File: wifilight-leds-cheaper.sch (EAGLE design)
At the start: 57 parts

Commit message: Damnit, how was I supposed to power this thing?
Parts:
- added +, -: (no value), adafruit:PINHD-1X1
- added D2: (no value), SparkFun-DiscreteSemi:DIODESOD123
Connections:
- new net N$18: +.1, D2.A
- net 12V: now also D2.C
- net GND: now also -.1
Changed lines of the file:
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@@
 <part name="R7" library="SparkFun-Passives" deviceset="RESISTOR" device="0402-RES" value="???"/>
 <part name="GND16" library="supply1" deviceset="GND" device=""/>
+<part name="+" library="adafruit" deviceset="PINHD-1X1" device=""/>
+<part name="-" library="adafruit" deviceset="PINHD-1X1" device=""/>
+<part name="D2" library="SparkFun-DiscreteSemi" deviceset="DIODE" device="SOD123"/>
+<part name="GND17" library="SparkFun-Aesthetics" deviceset="GND" device=""/>
+<part name="SUPPLY19" library="SparkFun-Aesthetics" deviceset="12V" device=""/>
 </parts>
 <sheets>
@@
 <instance part="R7" gate="G$1" x="17.78" y="114.3" rot="R270"/>
 <instance part="GND16" gate="1" x="17.78" y="93.98"/>
+<instance part="+" gate="G$1" x="-58.42" y="162.56"/>
+<instance part="-" gate="G$1" x="-58.42" y="147.32"/>
+<instance part="D2" gate="G$1" x="-76.2" y="162.56" rot="R180"/>
+<instance part="GND17" gate="1" x="-81.28" y="142.24"/>
+<instance part="SUPPLY19" gate="G$1" x="-86.36" y="165.1"/>
 </instances>
 <busses>
@@
 <wire x1="17.78" y1="96.52" x2="17.78" y2="99.06" width="0.1524" layer="91"/>
 </segment>
+<segment>
+<pinref part="-" gate="G$1" pin="1"/>
+<wire x1="-60.96" y1="147.32" x2="-81.28" y2="147.32" width="0.1524" layer="91"/>
+<pinref part="GND17" gate="1" pin="GND"/>
+<wire x1="-81.28" y1="147.32" x2="-81.28" y2="144.78" width="0.1524" layer="91"/>
+</segment>
 </net>
 <net name="SCL" class="0">
@@
 <pinref part="SUPPLY8" gate="G$1" pin="12V"/>
 <wire x1="-10.16" y1="116.84" x2="-10.16" y2="121.92" width="0.1524" layer="91"/>
+</segment>
+<segment>
+<pinref part="SUPPLY19" gate="G$1" pin="12V"/>
+<wire x1="-86.36" y1="165.1" x2="-86.36" y2="162.56" width="0.1524" layer="91"/>
+<pinref part="D2" gate="G$1" pin="C"/>
+<wire x1="-86.36" y1="162.56" x2="-78.74" y2="162.56" width="0.1524" layer="91"/>
 </segment>
 </net>
@@
 </segment>
 </net>
+<net name="N$18" class="0">
+<segment>
+<pinref part="D2" gate="G$1" pin="A"/>
+<pinref part="+" gate="G$1" pin="1"/>
+<wire x1="-73.66" y1="162.56" x2="-60.96" y2="162.56" width="0.1524" layer="91"/>
+</segment>
+</net>

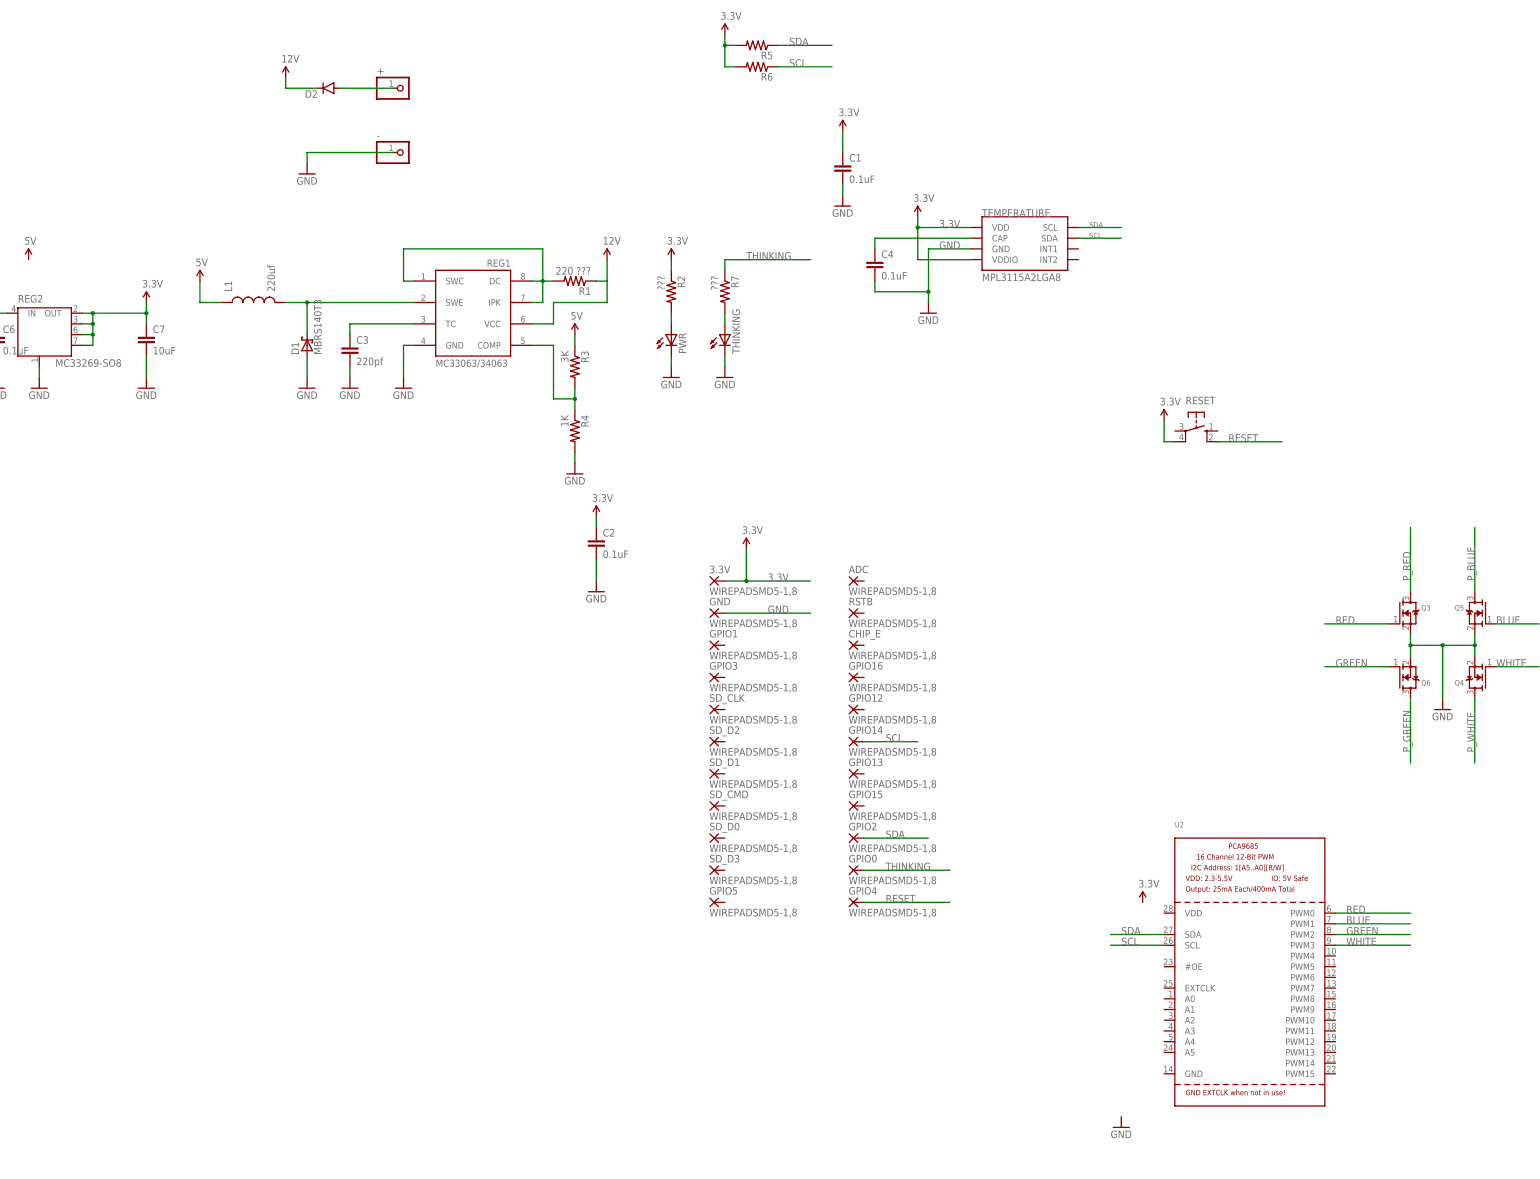
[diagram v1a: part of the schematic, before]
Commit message: As ordered recently. Discovered that SOT-23's are puny and 4 Luxeon Rebels are overkill. And that Banggood has cheaper ESP8266 modules.
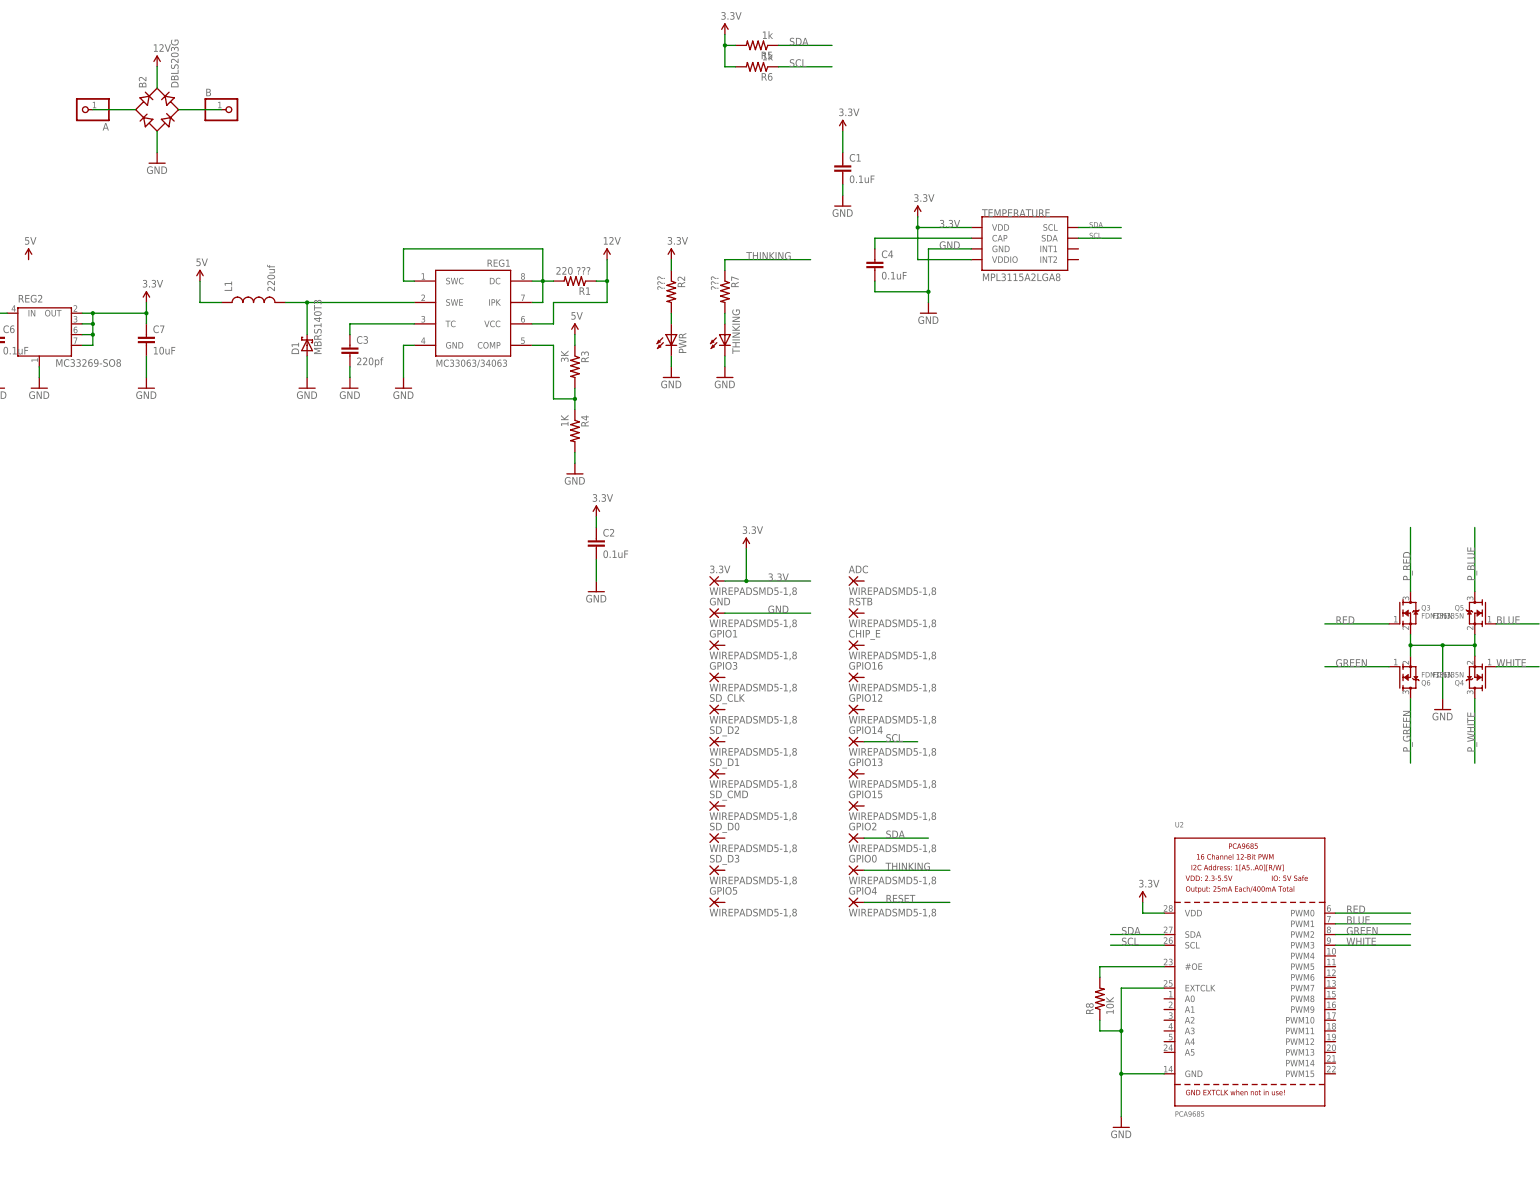
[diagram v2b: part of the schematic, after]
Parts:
- removed +, -: (no value), adafruit:PINHD-1X1
- removed D2: (no value), SparkFun-DiscreteSemi:DIODESOD123
- removed RESET: (no value), switch-omron:10-XX
- added A, B: (no value), adafruit:PINHD-1X1
- added B2: DBLS203G, rectifier:DBLS203G
- added R8: 10K, SparkFun-Resistors:10KOHM-1/10W-1%(0603)0603
- Q3, Q4, Q5, Q6: value (none) -> FDN335N
- R5, R6: value (none) -> 1k
- U2: value (none) -> PCA9685
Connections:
- new net N$19: B.1, B2.AC2
- new net N$20: R8.2, U2.#OE
- net 12V: now also B2.+; no longer D2.C
- net 3.3V: now also U2.VDD; no longer RESET.P1
- net GND: now also B2.-, R8.1, U2.EXTCLK, U2.GND; no longer -.1
- net N$18: now also A.1, B2.AC1; no longer +.1, D2.A
- net RESET: no longer RESET.S1
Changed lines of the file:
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@@
 <parts>
 <part name="C1" library="SparkFun-Passives" deviceset="CAP" device="0402-CAP" value="0.1uF"/>
-<part name="R5" library="SparkFun-Passives" deviceset="RESISTOR" device="0402-RES"/>
-<part name="R6" library="SparkFun-Passives" deviceset="RESISTOR" device="0402-RES"/>
+<part name="R5" library="SparkFun-Passives" deviceset="RESISTOR" device="0402-RES" value="1k"/>
+<part name="R6" library="SparkFun-Passives" deviceset="RESISTOR" device="0402-RES" value="1k"/>
 <part name="GND5" library="supply1" deviceset="GND" device=""/>
 <part name="3.3V" library="wirepad" deviceset="WIREPAD" device="SMD5-1,8"/>
@@
 <part name="GPIO0" library="wirepad" deviceset="WIREPAD" device="SMD5-1,8"/>
 <part name="GPIO4" library="wirepad" deviceset="WIREPAD" device="SMD5-1,8"/>
-<part name="U2" library="adafruit" deviceset="PCA9685" device=""/>
+<part name="U2" library="adafruit" deviceset="PCA9685" device="" value="PCA9685"/>
 <part name="GND1" library="SparkFun-Aesthetics" deviceset="GND" device=""/>
-<part name="Q3" library="adafruit" deviceset="MOSFET-N" device="WAVE"/>
-<part name="Q4" library="adafruit" deviceset="MOSFET-N" device="WAVE"/>
-<part name="Q5" library="adafruit" deviceset="MOSFET-N" device="WAVE"/>
-<part name="Q6" library="adafruit" deviceset="MOSFET-N" device="WAVE"/>
+<part name="Q3" library="adafruit" deviceset="MOSFET-N" device="WAVE" value="FDN335N"/>
+<part name="Q4" library="adafruit" deviceset="MOSFET-N" device="WAVE" value="FDN335N"/>
+<part name="Q5" library="adafruit" deviceset="MOSFET-N" device="WAVE" value="FDN335N"/>
+<part name="Q6" library="adafruit" deviceset="MOSFET-N" device="WAVE" value="FDN335N"/>
 <part name="LED1" library="led" deviceset="OVSTRGBBCR8" device=""/>
 <part name="LED2" library="led" deviceset="OVSTRGBBCR8" device=""/>
@@
 <part name="SUPPLY16" library="SparkFun-Aesthetics" deviceset="3.3V" device=""/>
 <part name="SUPPLY17" library="SparkFun-Aesthetics" deviceset="3.3V" device=""/>
-<part name="RESET" library="switch-omron" deviceset="10-XX" device=""/>
-<part name="SUPPLY18" library="SparkFun-Aesthetics" deviceset="3.3V" device=""/>
 <part name="THINKING" library="led" deviceset="LED" device="CHIP-LED0805"/>
 <part name="R7" library="SparkFun-Passives" deviceset="RESISTOR" device="0402-RES" value="???"/>
 <part name="GND16" library="supply1" deviceset="GND" device=""/>
-<part name="+" library="adafruit" deviceset="PINHD-1X1" device=""/>
-<part name="-" library="adafruit" deviceset="PINHD-1X1" device=""/>
-<part name="D2" library="SparkFun-DiscreteSemi" deviceset="DIODE" device="SOD123"/>
+<part name="A" library="adafruit" deviceset="PINHD-1X1" device=""/>
+<part name="B" library="adafruit" deviceset="PINHD-1X1" device=""/>
 <part name="GND17" library="SparkFun-Aesthetics" deviceset="GND" device=""/>
 <part name="SUPPLY19" library="SparkFun-Aesthetics" deviceset="12V" device=""/>
+<part name="B2" library="rectifier" deviceset="DB?*G" device="LS20" technology="3"/>
+<part name="R8" library="SparkFun-Resistors" deviceset="10KOHM-1/10W-1%(0603)" device="0603" value="10K"/>
 </parts>
 <sheets>
@@
 <instance part="SUPPLY16" gate="G$1" x="45.72" y="152.4"/>
 <instance part="SUPPLY17" gate="G$1" x="17.78" y="175.26"/>
-<instance part="RESET" gate="1" x="129.54" y="81.28" rot="R270"/>
-<instance part="SUPPLY18" gate="G$1" x="121.92" y="83.82"/>
 <instance part="THINKING" gate="G$1" x="17.78" y="104.14"/>
 <instance part="R7" gate="G$1" x="17.78" y="114.3" rot="R270"/>
 <instance part="GND16" gate="1" x="17.78" y="93.98"/>
-<instance part="+" gate="G$1" x="-58.42" y="162.56"/>
-<instance part="-" gate="G$1" x="-58.42" y="147.32"/>
-<instance part="D2" gate="G$1" x="-76.2" y="162.56" rot="R180"/>
-<instance part="GND17" gate="1" x="-81.28" y="142.24"/>
-<instance part="SUPPLY19" gate="G$1" x="-86.36" y="165.1"/>
+<instance part="A" gate="G$1" x="-134.62" y="157.48" rot="R180"/>
+<instance part="B" gate="G$1" x="-99.06" y="157.48"/>
+<instance part="GND17" gate="1" x="-116.84" y="144.78"/>
+<instance part="SUPPLY19" gate="G$1" x="-116.84" y="167.64"/>
+<instance part="B2" gate="G$1" x="-116.84" y="157.48" rot="R90"/>
+<instance part="R8" gate="G$1" x="106.68" y="-53.34" rot="R90"/>
 </instances>
 <busses>
@@
 </segment>
 <segment>
-<pinref part="-" gate="G$1" pin="1"/>
-<wire x1="-60.96" y1="147.32" x2="-81.28" y2="147.32" width="0.1524" layer="91"/>
 <pinref part="GND17" gate="1" pin="GND"/>
-<wire x1="-81.28" y1="147.32" x2="-81.28" y2="144.78" width="0.1524" layer="91"/>
+<wire x1="-116.84" y1="152.4" x2="-116.84" y2="147.32" width="0.1524" layer="91"/>
+<pinref part="B2" gate="G$1" pin="-"/>
+</segment>
+<segment>
+<pinref part="U2" gate="G$1" pin="GND"/>
+<pinref part="GND3" gate="1" pin="GND"/>
+<wire x1="121.92" y1="-71.12" x2="111.76" y2="-71.12" width="0.1524" layer="91"/>
+<wire x1="111.76" y1="-71.12" x2="111.76" y2="-81.28" width="0.1524" layer="91"/>
+<pinref part="U2" gate="G$1" pin="EXTCLK"/>
+<wire x1="121.92" y1="-50.8" x2="111.76" y2="-50.8" width="0.1524" layer="91"/>
+<wire x1="111.76" y1="-50.8" x2="111.76" y2="-60.96" width="0.1524" layer="91"/>
+<pinref part="R8" gate="G$1" pin="1"/>
+<wire x1="111.76" y1="-60.96" x2="111.76" y2="-71.12" width="0.1524" layer="91"/>
+<wire x1="106.68" y1="-58.42" x2="106.68" y2="-60.96" width="0.1524" layer="91"/>
+<wire x1="106.68" y1="-60.96" x2="111.76" y2="-60.96" width="0.1524" layer="91"/>
+<junction x="111.76" y="-71.12"/>
+<junction x="111.76" y="-60.96"/>
 </segment>
 </net>
@@
 <pinref part="SUPPLY8" gate="G$1" pin="12V"/>
 <wire x1="-10.16" y1="116.84" x2="-10.16" y2="121.92" width="0.1524" layer="91"/>
-</segment>
-<segment>
+<junction x="-10.16" y="116.84"/>
+</segment>
+<segment>
+<wire x1="-116.84" y1="162.56" x2="-116.84" y2="167.64" width="0.1524" layer="91"/>
 <pinref part="SUPPLY19" gate="G$1" pin="12V"/>
-<wire x1="-86.36" y1="165.1" x2="-86.36" y2="162.56" width="0.1524" layer="91"/>
-<pinref part="D2" gate="G$1" pin="C"/>
-<wire x1="-86.36" y1="162.56" x2="-78.74" y2="162.56" width="0.1524" layer="91"/>
+<pinref part="B2" gate="G$1" pin="+"/>
 </segment>
 </net>
@@
 </segment>
 <segment>
-<pinref part="RESET" gate="1" pin="P1"/>
-<wire x1="124.46" y1="78.74" x2="121.92" y2="78.74" width="0.1524" layer="91"/>
-<pinref part="SUPPLY18" gate="G$1" pin="3.3V"/>
-<wire x1="121.92" y1="78.74" x2="121.92" y2="83.82" width="0.1524" layer="91"/>
+<pinref part="U2" gate="G$1" pin="VDD"/>
+<wire x1="121.92" y1="-33.02" x2="116.84" y2="-33.02" width="0.1524" layer="91"/>
+<pinref part="SUPPLY5" gate="G$1" pin="3.3V"/>
+<wire x1="116.84" y1="-33.02" x2="116.84" y2="-30.48" width="0.1524" layer="91"/>
 </segment>
 </net>
@@
 <net name="RESET" class="0">
 <segment>
-<pinref part="RESET" gate="1" pin="S1"/>
-<wire x1="134.62" y1="78.74" x2="149.86" y2="78.74" width="0.1524" layer="91"/>
-<label x="137.16" y="78.74" size="1.778" layer="95"/>
-</segment>
-<segment>
 <pinref part="GPIO4" gate="G$1" pin="P"/>
 <wire x1="50.8" y1="-30.48" x2="71.12" y2="-30.48" width="0.1524" layer="91"/>
@@
 </segment>
 </net>
+<net name="N$19" class="0">
+<segment>
+<pinref part="B" gate="G$1" pin="1"/>
+<wire x1="-111.76" y1="157.48" x2="-101.6" y2="157.48" width="0.1524" layer="91"/>
+<pinref part="B2" gate="G$1" pin="AC2"/>
+</segment>
+</net>
 <net name="N$18" class="0">
 <segment>
-<pinref part="D2" gate="G$1" pin="A"/>
-<pinref part="+" gate="G$1" pin="1"/>
-<wire x1="-73.66" y1="162.56" x2="-60.96" y2="162.56" width="0.1524" layer="91"/>
-</segment>
-</net>
+<pinref part="A" gate="G$1" pin="1"/>
+<wire x1="-132.08" y1="157.48" x2="-121.92" y2="157.48" width="0.1524" layer="91"/>
+<pinref part="B2" gate="G$1" pin="AC1"/>
+</segment>
+</net>
+<net name="N$20" class="0">
+<segment>
+<pinref part="U2" gate="G$1" pin="#OE"/>
+<wire x1="121.92" y1="-45.72" x2="106.68" y2="-45.72" width="0.1524" layer="91"/>
+<pinref part="R8" gate="G$1" pin="2"/>
+<wire x1="106.68" y1="-45.72" x2="106.68" y2="-48.26" width="0.1524" layer="91"/>
+</segment>
+</net>

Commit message: Mk2
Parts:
- removed 3.3V, ADC, CHIP_E, GND, GPIO0, GPIO1, GPIO12, GPIO13, GPIO14, GPIO15, GPIO16, GPIO2, GPIO3, GPIO4, GPIO5, RSTB, SD_CLK, SD_CMD, SD_D0, SD_D1, SD_D2, SD_D3: WIREPADSMD5-1,8, wirepad:WIREPADSMD5-1,8
- removed LED4: OVSTRGBBCR8, led:OVSTRGBBCR8
- removed Q5, Q6: FDN335N, adafruit:MOSFET-NWAVE
- removed U$4: LUXEON-REBEL, SparkFun-LED:LUXEON-REBEL
- added MPU: ESP8266_ESP-12, ESP8266-ESP12:ESP8266_ESP-12
- added Q1, Q2: BUK98180-100A, nxp_60:BUK98180-100A
- C1, C2, C3: device SparkFun-Passives:CAP0402-CAP -> resistor:C-EUC0805K
- C4, C6: device SparkFun-Capacitors:0.1UF-16V(+-10%)(0402) -> resistor:C-EUC0805K
- C7: device SparkFun-Capacitors:10UF-6.3V-20%(1206) -> resistor:C-EUC0805K
- Q3, Q4: value FDN335N -> BUK98180-100A; device adafruit:MOSFET-NWAVE -> nxp_60:BUK98180-100A
- R1, R2, R3, R4, R5, R6, R7: device SparkFun-Passives:RESISTOR0402-RES -> resistor:R-EU_R0805
- R8: device SparkFun-Resistors:10KOHM-1/10W-1%(0603)0603 -> resistor:R-EU_R0805
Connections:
- removed net N$12: U$3.C, U$4.A
- removed net N$3: LED3-G.C, LED4-G.A
- removed net N$4: LED3-R.C, LED4-R.A
- removed net N$9: LED3G$1.C, LED4G$1.A
- new net N$25: MPU.GPIO14
- new net N$26: MPU.GPIO16
- new net N$27: MPU.CH_PD
- new net N$28: MPU.ADC
- new net N$29: MPU.REST
- new net N$32: MPU.GPIO4
- new net N$33: MPU.GPIO0
- new net N$34: MPU.GPIO2
- new net N$35: MPU.GPIO15
- new net N$36: MPU.GPIO5
- net 3.3V: now also MPU.VCC; no longer 3.3V.P
- net BLUE: now also Q2.G; no longer Q5.G
- net GND: now also MPU.GND, Q1.S, Q2.S; no longer GND.P, Q5.S, Q6.S, U$4.S
- net GREEN: now also Q4.G, U2.PWM3; no longer Q6.G, U2.PWM2
- net P_BLUE: now also LED3G$1.C, Q2.D; no longer LED4G$1.C, Q5.D
- net P_GREEN: now also LED3-G.C, Q4.D; no longer LED4-G.C, Q6.D
- net P_RED: now also LED3-R.C; no longer LED4-R.C
- net P_WHITE: now also Q1.D, U$3.C; no longer Q4.D, U$4.C
- net RED: now also U2.PWM2; no longer U2.PWM0
- net RESET: now also MPU.TXD; no longer GPIO4.P
- net SCL: now also MPU.GPIO13; no longer GPIO14.P
- net SDA: now also MPU.GPIO12; no longer GPIO2.P
- net THINKING: now also MPU.RXD; no longer GPIO0.P
- net WHITE: now also Q1.G, U2.PWM0; no longer Q4.G, U2.PWM3
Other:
- moved on the sheet: C1, C2, C3, C4, C6, C7
